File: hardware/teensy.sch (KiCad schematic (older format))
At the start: 20 parts

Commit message: Working on schematic
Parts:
- added C5, C7, C8: 2.2u, symbol C
- added F1: FUSE, symbol FUSE
- added L1: 600 Ohm/100 Mhz, symbol INDUCTOR_SMALL
- added U3: LP38691, symbol LP38691
- C12, C13, C14, C15: renamed from C?; footprint (none) -> Capacitors_SMD:C_0603
- C16: renamed from C?; value 0.1u -> 2.2u; footprint (none) -> Capacitors_SMD:C_0603
- U4: renamed from U?; footprint MODULE -> Housings_DFN_QFN:QFN-16-1EP_3x3mm_Pitch0.5mm
- U5: renamed from U?; footprint MODULE -> Housings_QFP:LQFP-64_10x10mm_Pitch0.5mm
- gave numbers to parts that had none: 13
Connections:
- net +3V3: now also C7.1, U3.4 (OUT), U3.5 (SNS)
- net GND: now also C5.2, C7.2, C8.2, L1.2, U3.2 (GND), U3.7 (GND); no longer P5.6 (shield)
- net VUSB: no longer names the net of P5.1 (VCC)
- net VUSB: now also C8.1, F1.1
- new net: L1.1, P5.6 (shield)
- new net +5V: C5.1, F1.2, U3.1 (IN), U3.6 (IN)
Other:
- moved on the sheet: C12, C13, C14, C15, C16, C6

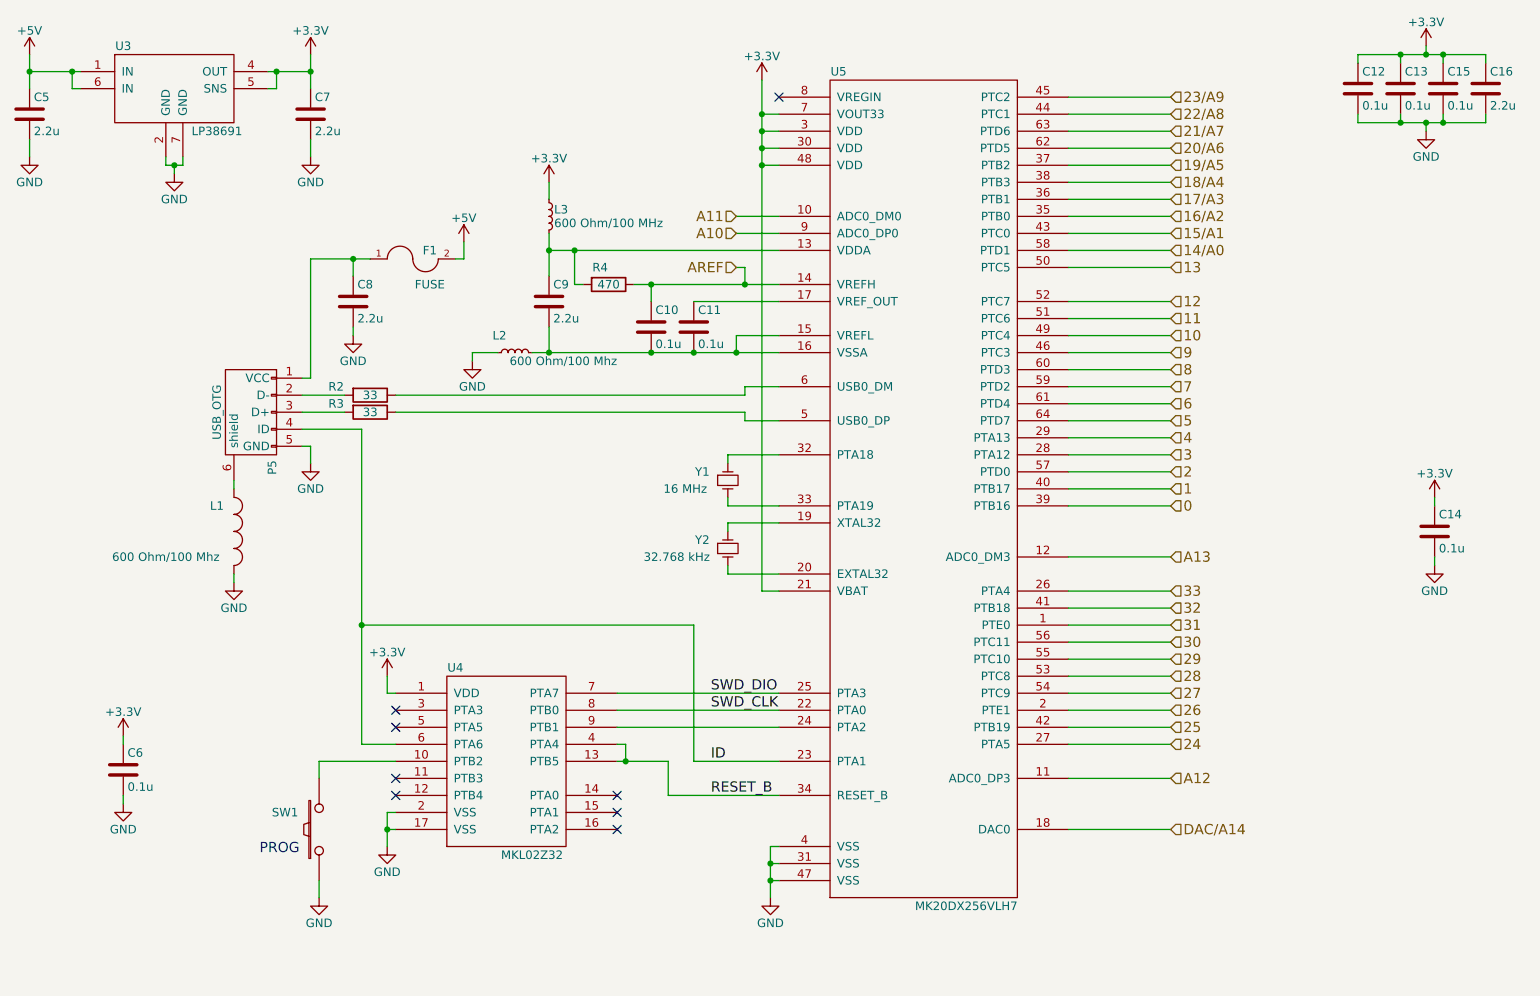
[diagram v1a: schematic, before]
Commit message: Created schematic PDF.  Working on BOM.
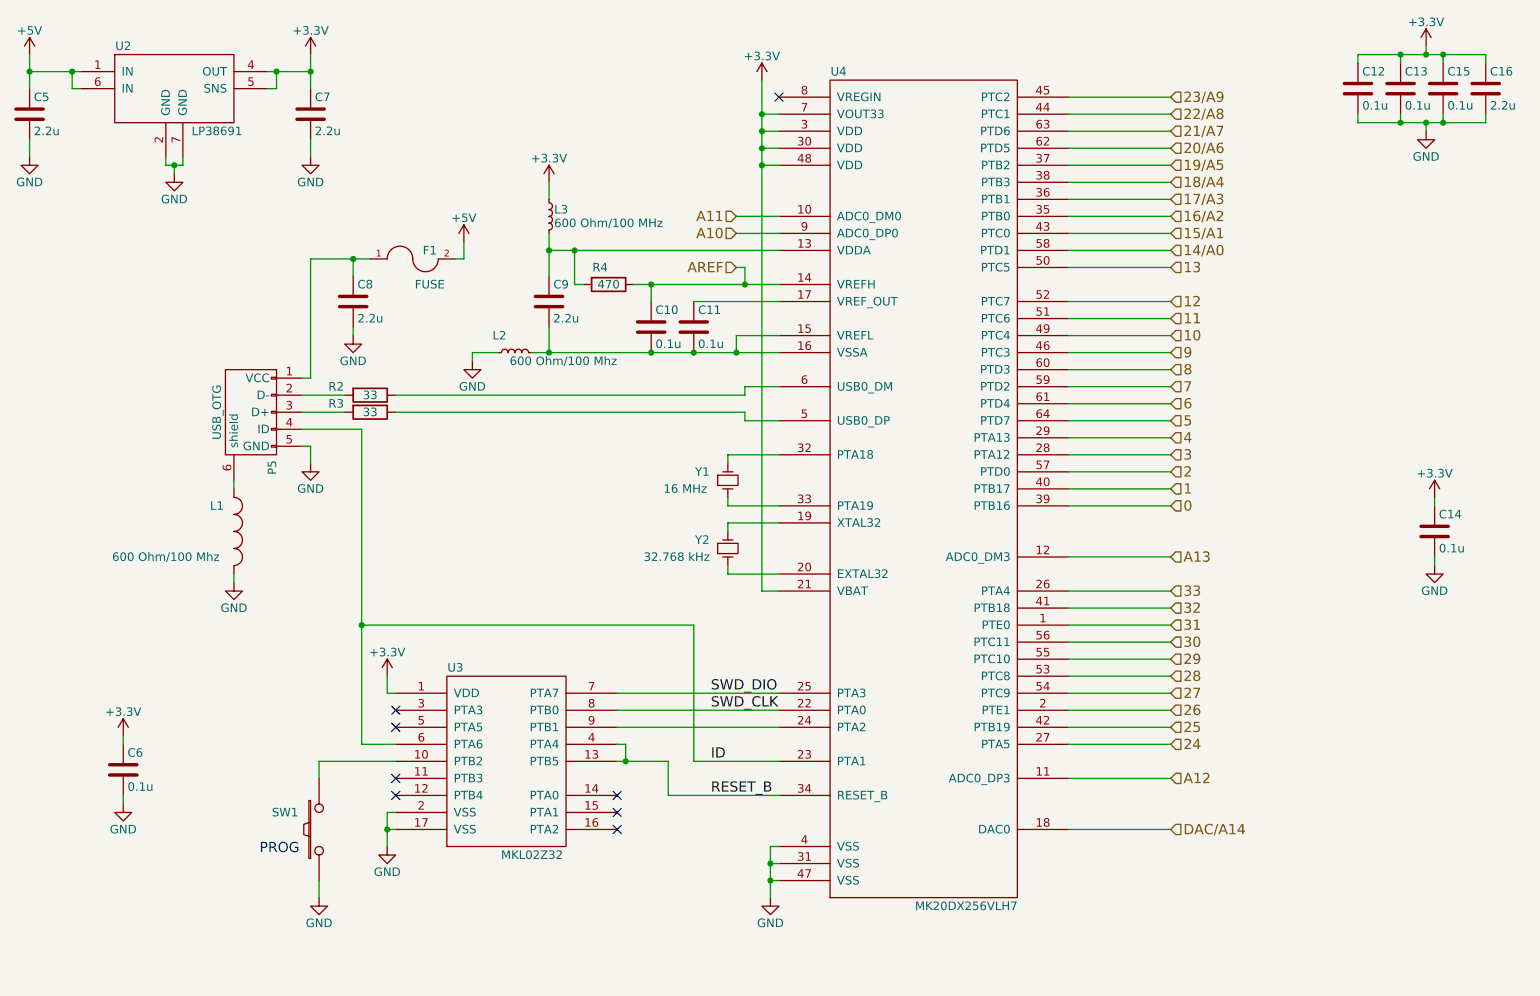
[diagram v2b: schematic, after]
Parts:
- renumbered U3 to U2, U4 to U3, U5 to U4
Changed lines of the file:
@@
 $EndDescr
 $Comp
-L MK20DX256VLH7 U5
+L MK20DX256VLH7 U4
 U 1 1 57630F8F
 P 6700 2950
-F 0 "U5" H 6200 4750 50  0000 C CNN
+F 0 "U4" H 6200 4750 50  0000 C CNN
 F 1 "MK20DX256VLH7" H 6950 -150 50  0000 C CNN
 F 2 "Housings_QFP:LQFP-64_10x10mm_Pitch0.5mm" H 6550 3050 50  0001 C CNN
@@
 $EndComp
 $Comp
-L MKL02Z32 U4
+L MKL02Z32 U3
 U 1 1 57630F96
 P 4250 5250
-F 0 "U4" H 3950 5850 50  0000 C CNN
+F 0 "U3" H 3950 5850 50  0000 C CNN
 F 1 "MKL02Z32" H 4400 4750 50  0000 C CNN
 F 2 "Housings_DFN_QFN:QFN-16-1EP_3x3mm_Pitch0.5mm" H 4250 5350 50  0001 C CNN
@@
 $EndComp
 $Comp
-L LP38691 U3
+L LP38691 U2
 U 1 1 57640637
 P 2300 1250
-F 0 "U3" H 2000 1500 50  0000 C CNN
+F 0 "U2" H 2000 1500 50  0000 C CNN
 F 1 "LP38691" H 2550 1000 50  0000 C CNN
 F 2 "" H 2300 1250 60  0000 C CNN

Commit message: Working on BOM.
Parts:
- removed C8: 2.2u, symbol C
- removed F1: FUSE, symbol FUSE
- removed L1: 600 Ohm/100 Mhz, symbol INDUCTOR_SMALL
- added L1: 600 Ohm/100 MHz, Resistors_SMD:R_0603, symbol L_Small
- C10: renamed from C11; footprint (none) -> Capacitors_SMD:C_0603
- C5, C6, C7: footprint (none) -> Capacitors_SMD:C_0603
- C8: renamed from C9; footprint (none) -> Capacitors_SMD:C_0603
- C9: renamed from C10; footprint (none) -> Capacitors_SMD:C_0603
- L2, L3, R2, R3: footprint (none) -> Resistors_SMD:R_0603
- SW1: footprint (none) -> Buttons_Switches_SMD:SW_SPST_KMR2
- U2: footprint (none) -> Housings_DFN_QFN:DFN-6-1EP_3x3mm_Pitch0.95mm
- Y1: footprint (none) -> Crystals:Crystal_SMD_2520_4Pads
- renumbered C12 to C11, C13 to C12, C14 to C13, C15 to C14, C16 to C15
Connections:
- net +5V: now also P5.1 (VCC)
- net GND: now also L1.2
- net at P5.6 (shield): now also L1.1

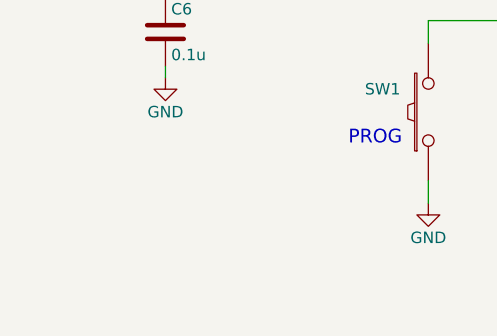
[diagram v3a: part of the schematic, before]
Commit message: Added piezo transducer.  Working on footprints
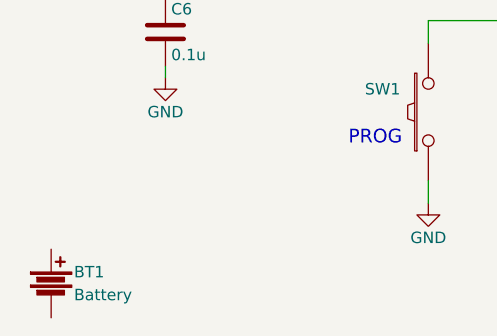
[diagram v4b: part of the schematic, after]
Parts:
- added BT1: Battery, symbol Battery
- Y2: footprint (none) -> footprint:ABS07
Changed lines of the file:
@@
 $EndComp
 $Comp
-L GND #PWR30
+L GND #PWR31
 U 1 1 57630FB2
 P 3550 5700
-F 0 "#PWR30" H 3550 5450 50  0001 C CNN
+F 0 "#PWR31" H 3550 5450 50  0001 C CNN
 F 1 "GND" H 3550 5550 50  0000 C CNN
 F 2 "" H 3550 5700 50  0000 C CNN
@@
 $EndComp
 $Comp
-L +3.3V #PWR29
+L +3.3V #PWR30
 U 1 1 57630FBC
 P 3550 4700
-F 0 "#PWR29" H 3550 4550 50  0001 C CNN
+F 0 "#PWR30" H 3550 4550 50  0001 C CNN
 F 1 "+3.3V" H 3550 4840 50  0000 C CNN
 F 2 "" H 3550 4700 50  0000 C CNN
@@
 $EndComp
 $Comp
-L GND #PWR34
+L GND #PWR35
 U 1 1 57630FC2
 P 5800 6000
-F 0 "#PWR34" H 5800 5750 50  0001 C CNN
+F 0 "#PWR35" H 5800 5750 50  0001 C CNN
 F 1 "GND" H 5800 5850 50  0000 C CNN
 F 2 "" H 5800 6000 50  0000 C CNN
@@
 $EndComp
 $Comp
-L GND #PWR28
+L GND #PWR29
 U 1 1 57630FD0
 P 3150 6000
-F 0 "#PWR28" H 3150 5750 50  0001 C CNN
+F 0 "#PWR29" H 3150 5750 50  0001 C CNN
 F 1 "GND" H 3150 5850 50  0000 C CNN
 F 2 "" H 3150 6000 50  0000 C CNN
@@
 NoConn ~ 4900 5400
 $Comp
-L +3.3V #PWR33
+L +3.3V #PWR34
 U 1 1 57630FE2
 P 5750 1200
-F 0 "#PWR33" H 5750 1050 50  0001 C CNN
+F 0 "#PWR34" H 5750 1050 50  0001 C CNN
 F 1 "+3.3V" H 5750 1340 50  0000 C CNN
 F 2 "" H 5750 1200 50  0000 C CNN
@@
 F 0 "Y2" V 5500 3800 50  0000 C CNN
 F 1 "32.768 kHz" V 5600 3650 50  0000 C CNN
-F 2 "" H 5550 3950 50  0000 C CNN
+F 2 "footprint:ABS07" H 5550 3950 50  0001 C CNN
 F 3 "" H 5550 3950 50  0000 C CNN
 	1    5550 3950
@@
 $EndComp
 $Comp
-L GND #PWR21
+L GND #PWR22
 U 1 1 57631016
 P 2000 5450
-F 0 "#PWR21" H 2000 5200 50  0001 C CNN
+F 0 "#PWR22" H 2000 5200 50  0001 C CNN
 F 1 "GND" H 2000 5300 50  0000 C CNN
 F 2 "" H 2000 5450 50  0000 C CNN
@@
 $EndComp
 $Comp
-L +3.3V #PWR20
+L +3.3V #PWR21
 U 1 1 5763101C
 P 2000 5050
-F 0 "#PWR20" H 2000 4900 50  0001 C CNN
+F 0 "#PWR21" H 2000 4900 50  0001 C CNN
 F 1 "+3.3V" H 2000 5190 50  0000 C CNN
 F 2 "" H 2000 5050 50  0000 C CNN
@@
 $EndComp
 $Comp
-L GND #PWR38
+L GND #PWR39
 U 1 1 5763102B
 P 9700 4050
-F 0 "#PWR38" H 9700 3800 50  0001 C CNN
+F 0 "#PWR39" H 9700 3800 50  0001 C CNN
 F 1 "GND" H 9700 3900 50  0000 C CNN
 F 2 "" H 9700 4050 50  0000 C CNN
@@
 $EndComp
 $Comp
-L +3.3V #PWR37
+L +3.3V #PWR38
 U 1 1 57631031
 P 9700 3650
-F 0 "#PWR37" H 9700 3500 50  0001 C CNN
+F 0 "#PWR38" H 9700 3500 50  0001 C CNN
 F 1 "+3.3V" H 9700 3790 50  0000 C CNN
 F 2 "" H 9700 3650 50  0000 C CNN
@@
 $EndComp
 $Comp
-L GND #PWR31
+L GND #PWR32
 U 1 1 57631066
 P 4050 2850
-F 0 "#PWR31" H 4050 2600 50  0001 C CNN
+F 0 "#PWR32" H 4050 2600 50  0001 C CNN
 F 1 "GND" H 4050 2700 50  0000 C CNN
 F 2 "" H 4050 2850 50  0000 C CNN
@@
 $EndComp
 $Comp
-L +3.3V #PWR32
+L +3.3V #PWR33
 U 1 1 57631075
 P 4500 1800
-F 0 "#PWR32" H 4500 1650 50  0001 C CNN
+F 0 "#PWR33" H 4500 1650 50  0001 C CNN
 F 1 "+3.3V" H 4500 1940 50  0000 C CNN
 F 2 "" H 4500 1800 50  0000 C CNN
@@
 $EndComp
 $Comp
-L +3.3V #PWR35
+L +3.3V #PWR36
 U 1 1 57631098
 P 9650 1000
-F 0 "#PWR35" H 9650 850 50  0001 C CNN
+F 0 "#PWR36" H 9650 850 50  0001 C CNN
 F 1 "+3.3V" H 9650 1140 50  0000 C CNN
 F 2 "" H 9650 1000 50  0000 C CNN
@@
 $EndComp
 $Comp
-L GND #PWR36
+L GND #PWR37
 U 1 1 5763109E
 P 9650 1500
-F 0 "#PWR36" H 9650 1250 50  0001 C CNN
+F 0 "#PWR37" H 9650 1250 50  0001 C CNN
 F 1 "GND" H 9650 1350 50  0000 C CNN
 F 2 "" H 9650 1500 50  0000 C CNN
@@
 $EndComp
 $Comp
-L GND #PWR23
+L GND #PWR24
 U 1 1 57632880
 P 2650 3950
-F 0 "#PWR23" H 2650 3700 50  0001 C CNN
+F 0 "#PWR24" H 2650 3700 50  0001 C CNN
 F 1 "GND" H 2650 3800 50  0000 C CNN
 F 2 "" H 2650 3950 50  0000 C CNN
@@
 $EndComp
 $Comp
-L GND #PWR27
+L GND #PWR28
 U 1 1 576328C7
 P 3100 3450
-F 0 "#PWR27" H 3100 3200 50  0001 C CNN
+F 0 "#PWR28" H 3100 3200 50  0001 C CNN
 F 1 "GND" H 3100 3300 50  0000 C CNN
 F 2 "" H 3100 3450 50  0000 C CNN
@@
 $EndComp
 $Comp
-L +5V #PWR26
+L +5V #PWR27
 U 1 1 5763FF76
 P 3100 2850
-F 0 "#PWR26" H 3100 2700 50  0001 C CNN
+F 0 "#PWR27" H 3100 2700 50  0001 C CNN
 F 1 "+5V" H 3100 2990 50  0000 C CNN
 F 2 "" H 3100 2850 50  0000 C CNN
@@
 $EndComp
 $Comp
-L +5V #PWR18
+L +5V #PWR19
 U 1 1 57640ACB
 P 1450 1050
-F 0 "#PWR18" H 1450 900 50  0001 C CNN
+F 0 "#PWR19" H 1450 900 50  0001 C CNN
 F 1 "+5V" H 1450 1190 50  0000 C CNN
 F 2 "" H 1450 1050 50  0000 C CNN
@@
 $EndComp
 $Comp
-L +3.3V #PWR24
+L +3.3V #PWR25
 U 1 1 57641034
 P 3100 1050
-F 0 "#PWR24" H 3100 900 50  0001 C CNN
+F 0 "#PWR25" H 3100 900 50  0001 C CNN
 F 1 "+3.3V" H 3100 1190 50  0000 C CNN
 F 2 "" H 3100 1050 50  0000 C CNN
@@
 $EndComp
 $Comp
-L GND #PWR25
+L GND #PWR26
 U 1 1 57641148
 P 3100 1650
-F 0 "#PWR25" H 3100 1400 50  0001 C CNN
+F 0 "#PWR26" H 3100 1400 50  0001 C CNN
 F 1 "GND" H 3100 1500 50  0000 C CNN
 F 2 "" H 3100 1650 50  0000 C CNN
@@
 $EndComp
 $Comp
-L GND #PWR19
+L GND #PWR20
 U 1 1 5764119E
 P 1450 1650
-F 0 "#PWR19" H 1450 1400 50  0001 C CNN
+F 0 "#PWR20" H 1450 1400 50  0001 C CNN
 F 1 "GND" H 1450 1500 50  0000 C CNN
 F 2 "" H 1450 1650 50  0000 C CNN
@@
 $EndComp
 $Comp
-L GND #PWR22
+L GND #PWR23
 U 1 1 576416D5
 P 2300 1750
-F 0 "#PWR22" H 2300 1500 50  0001 C CNN
+F 0 "#PWR23" H 2300 1500 50  0001 C CNN
 F 1 "GND" H 2300 1600 50  0000 C CNN
 F 2 "" H 2300 1750 50  0000 C CNN
@@
 Wire Wire Line
 	2650 3950 2650 3900
+$Comp
+L Battery BT1
+U 1 1 5766CCF6
+P 1500 6350
+F 0 "BT1" H 1600 6400 50  0000 L CNN
+F 1 "Battery" H 1600 6300 50  0000 L CNN
+F 2 "" V 1500 6390 50  0000 C CNN
+F 3 "" V 1500 6390 50  0000 C CNN
+	1    1500 6350
+	1    0    0    -1
+$EndComp
 $EndSCHEMATC
